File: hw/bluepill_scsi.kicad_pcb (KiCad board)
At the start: 2 copper layers, 43.8 x 73.7 mm, 14 parts, among them J1 Micro_SD_Card, J2 Conn_02x25_Odd_Even, J3 Programming Pins, J4 Berg Power Connector, U1 BluePill_STM32F103C

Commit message: Initial 1.1-a
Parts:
- added G***: LOGO, BlueSCSILogo:dogcow, B.Cu at (95.3, 160.4)
- added G***: LOGO, BlueSCSILogo:mac_happy_small, F.Cu at (95.4, 160.3)
- added G***: LOGO, BlueSCSILogo:cc_by_nc_sa_front_silk_screen, B.Cu at (103.9, 149.4)
- added G***: LOGO, BlueSCSILogo:cc_by_nc_sa_small_front_silk_screen, F.Cu at (82.8, 112.9)
- added G***: LOGO, BlueSCSILogo:BlueSCSILogoFP, B.Cu at (93.2, 126.2)
- added H2: MountingHole_Pad, MountingHole:MountingHole_2.7mm_M2.5_Pad_Via, F.Cu at (84.3, 166.5)
- added J5: Micro_SD_Card, Connector_Card:microSD_HC_Molex_104031-0811, F.Cu at (96.0, 161.0)
- added R1: R_US, Resistor_THT:R_Axial_DIN0204_L3.6mm_D1.6mm_P5.08mm_Horizontal, F.Cu at (82.4, 151.8)
- added R2: R_US, Resistor_THT:R_Axial_DIN0204_L3.6mm_D1.6mm_P5.08mm_Horizontal, F.Cu at (82.4, 144.3)
- D4, D5: moved to F.Cu
- H1: footprint MountingHole:MountingHole_2.7mm_M2.5 -> MountingHole:MountingHole_2.7mm_M2.5_Pad_Via
- J1: value Micro_SD_Card -> Berg Power Connector; footprint Connector_Card:microSD_HC_Molex_104031-0811 -> 171825-4:TE_171825-4
- J3: value Programming Pins -> ACT_LED; footprint Connector_PinHeader_2.54mm:PinHeader_1x04_P2.54mm_Vertical -> Connector_PinSocket_2.54mm:PinSocket_1x02_P2.54mm_Vertical
- J4: value Berg Power Connector -> POWER_LED; footprint 171825-4:TE_171825-4 -> Connector_PinSocket_2.54mm:PinSocket_1x02_P2.54mm_Vertical
- moved D4 87.3 mm to (105.4, 161.2)
- moved D5 80.6 mm to (105.4, 157.7)
- moved U1 73.1 mm to (101.0, 151.8), turned to 180 degrees
- moved JP1 70.5 mm to (111.1, 151.6), turned to 0 degrees
- moved JP2 70.5 mm to (107.3, 151.6), turned to 0 degrees
- moved J2 41.6 mm to (118.7, 102.2), turned to 0 degrees
- moved J1 33.5 mm to (105.2, 165.6), turned to 0 degrees
- moved H1 22.1 mm to (84.3, 98.9)
- moved J3 18.0 mm to (83.2, 161.5), turned to 90 degrees
- moved J4 17.1 mm to (83.2, 157.9), turned to 90 degrees
- moved RN3 15.3 mm to (107.3, 125.1), turned to 270 degrees
- moved RN4 15.3 mm to (111.1, 125.1), turned to 270 degrees
- moved RN1 15.3 mm to (107.3, 98.4)
- moved RN2 15.3 mm to (111.1, 98.4)
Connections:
- J1 pad 1: Net-(J1-Pad1) -> +5V
- J1 pad 2: /SD_CS -> GND
- J1 pad 3: /SD_MOSI -> (no net)
- J1 pad 4: +3V3 -> (no net)
- J2 pad 25: Net-(J2-Pad25) -> (no net)
- J2 pad 34: Net-(J2-Pad34) -> (no net)
- J3 pad 1: +3V3 -> Net-(J3-Pad1)
- J4 pad 1: +5V -> Net-(J4-Pad1)
- RN1 pad 10: /SCSI_ATN -> /SCSI_DAT7
- RN1 pad 2: /SCSI_IO -> /SCSI_DAT0
- RN1 pad 3: /SCSI_REQ -> /SCSI_DAT1
- RN1 pad 4: /SCSI_CD -> /SCSI_DAT3
- RN1 pad 5: /SCSI_MSG -> /SCSI_DAT2
- RN1 pad 6: /SCSI_BSY -> /SCSI_DBP
- RN1 pad 7: /SCSI_SEL -> /SCSI_DAT4
- RN1 pad 8: /SCSI_RST -> /SCSI_DAT5
- RN1 pad 9: /SCSI_ACK -> /SCSI_DAT6
- RN2 pad 10: /SCSI_ATN -> /SCSI_DAT7
- RN2 pad 2: /SCSI_IO -> /SCSI_DAT0
- RN2 pad 3: /SCSI_REQ -> /SCSI_DAT1
- RN2 pad 4: /SCSI_CD -> /SCSI_DAT3
- RN2 pad 5: /SCSI_MSG -> /SCSI_DAT2
- RN2 pad 6: /SCSI_BSY -> /SCSI_DBP
- RN2 pad 7: /SCSI_SEL -> /SCSI_DAT4
- RN2 pad 8: /SCSI_RST -> /SCSI_DAT5
- RN2 pad 9: /SCSI_ACK -> /SCSI_DAT6
- RN3 pad 10: /SCSI_DAT7 -> /SCSI_IO
- RN3 pad 2: /SCSI_DBP -> /SCSI_ATN
- RN3 pad 3: /SCSI_DAT0 -> /SCSI_BSY
- RN3 pad 4: /SCSI_DAT1 -> /SCSI_ACK
- RN3 pad 5: /SCSI_DAT2 -> /SCSI_RST
- RN3 pad 6: /SCSI_DAT3 -> /SCSI_MSG
- RN3 pad 7: /SCSI_DAT4 -> /SCSI_SEL
- RN3 pad 8: /SCSI_DAT5 -> /SCSI_CD
- RN3 pad 9: /SCSI_DAT6 -> /SCSI_REQ
- RN4 pad 10: /SCSI_DAT7 -> /SCSI_IO
- RN4 pad 2: /SCSI_DBP -> /SCSI_ATN
- RN4 pad 3: /SCSI_DAT0 -> /SCSI_BSY
- RN4 pad 4: /SCSI_DAT1 -> /SCSI_ACK
- RN4 pad 5: /SCSI_DAT2 -> /SCSI_RST
- RN4 pad 6: /SCSI_DAT3 -> /SCSI_MSG
- RN4 pad 7: /SCSI_DAT4 -> /SCSI_SEL
- RN4 pad 8: /SCSI_DAT5 -> /SCSI_CD
- RN4 pad 9: /SCSI_DAT6 -> /SCSI_REQ
- U1 pad 1: Net-(U1-Pad1) -> (no net)
- U1 pad 14: Net-(U1-Pad14) -> (no net)
- U1 pad 17: Net-(U1-Pad17) -> (no net)
- U1 pad 2: /LED -> (no net)
- U1 pad 28: Net-(U1-Pad28) -> (no net)
- U1 pad 29: Net-(U1-Pad29) -> (no net)
- U1 pad 3: Net-(U1-Pad3) -> (no net)
- U1 pad 4: Net-(U1-Pad4) -> (no net)
- U1 pad 5: Net-(U1-Pad5) -> /EXTERNAL_LED
- U1 pad 6: Net-(U1-Pad6) -> (no net)
- U1 pad 7: Net-(U1-Pad7) -> (no net)
- U1 pad 8: Net-(U1-Pad8) -> (no net)
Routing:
- net +5V: track 108.7 -> 9.72 mm
- net +3V3: track 85.0 -> 27.0 mm, vias 0 -> 1
- net /SCSI_BSY: track 101.0 -> 51.2 mm
- net /SCSI_ACK: track 85.7 -> 51.2 mm, vias 1 -> 0
- net /SCSI_CD: track 23.0 -> 49.1 mm
- net /SCSI_IO: track 23.0 -> 49.1 mm
- net /SCSI_REQ: track 23.4 -> 49.2 mm
- net /EXTERNAL_LED: track 0.00 -> 24.8 mm, vias 0 -> 1
- net /SCSI_RST: track 24.6 -> 49.1 mm
- net /SCSI_MSG: track 24.6 -> 49.1 mm, vias 1 -> 0
- net /TERM_PWR: track 63.5 -> 39.4 mm, vias 0 -> 1
- net /SCSI_ATN: track 26.3 -> 48.6 mm
- net /SCSI_SEL: track 27.5 -> 49.1 mm
- net Net-(J3-Pad1): track 0.00 -> 18.6 mm
- net /SCSI_DAT2: track 42.8 -> 24.8 mm, vias 1 -> 0
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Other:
- board text added: "+"
- board text added: "+3V3"
- board text added: "-"
- board text added: "12V(Y)"
- board text added: "500-1kΩ"
- board text added: "5V(R)"
- board text added: "ACT"
- board text added: "BADWOLF"
- board text added: "BERG"
- board text added: "BlueSCSI 1.1-a"
- board text added: "BlueSCSI(TM) © Eric Helgeson github.com/erichelgeson/bluescsi"
- board text added: "BlueSCSI(TM) © Eric Helgeson https://github.com/erichelgeson/bluescsi"
- board text added: "G"
- board text added: "GND"
- board text added: "LED"
- board text added: "NOT FOR COMMERCIAL SALE"
- board text added: "PA1"
- board text added: "PA4"
- board text added: "PA7"
- board text added: "PA8"
- board text added: "PB15"
- board text added: "PC13"
- board text added: "PC14"
- board text added: "PC15"
- board text added: "PWR"
- board text added: "RN1 220Ω"
- board text added: "RN2 330Ω"
- board text added: "RN3 220Ω"
- board text added: "RN4 330Ω"
- board text added: "RX2"
- board text added: "SCSI_ACK"
- board text added: "SCSI_ATN"
- board text added: "SCSI_BSY"
- board text added: "SCSI_CD"
- board text added: "SCSI_DAT0"
- board text added: "SCSI_DAT1"
- board text added: "SCSI_DAT2"
- board text added: "SCSI_DAT3"
- board text added: "SCSI_DAT4"
- board text added: "SCSI_DAT5"
- board text added: "SCSI_DAT6"
- board text added: "SCSI_DAT7"
- board text added: "SCSI_DBP"
- board text added: "SCSI_IO"
- board text added: "SCSI_MSG"
- board text added: "SCSI_REQ"
- board text added: "SCSI_RST"
- board text added: "SCSI_SEL"
- board text added: "SD_CLK"
- board text added: "SD_CS"
- board text added: "SD_MISO"
- board text added: "SD_MOSI"
- board text added: "TX2"
- board text added: "USB HERE"
- board text added: "VCC"
- board text added: "https://scsi.blue/"
- board text removed: "220"
- board text removed: "3.3 G TX RX"
- board text removed: "330"
- board text removed: "BlueSCSI 1.0-c"

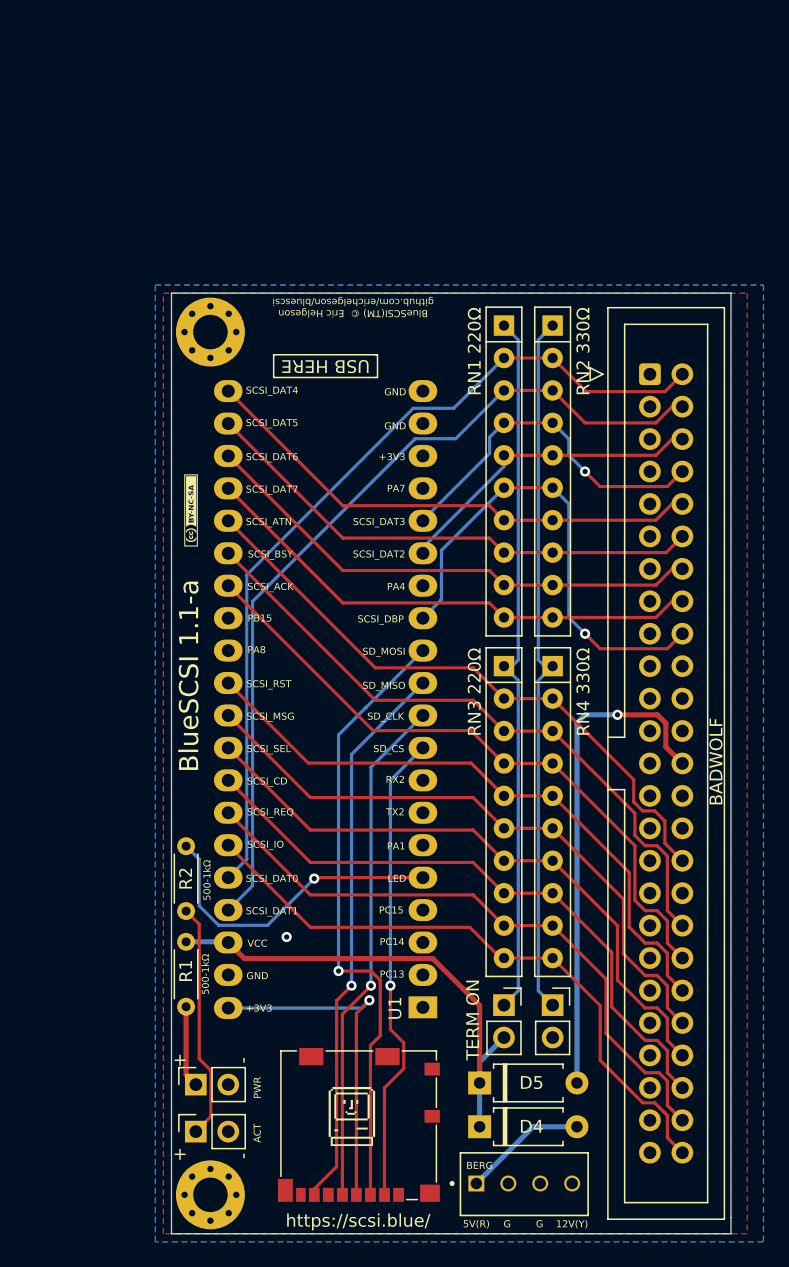
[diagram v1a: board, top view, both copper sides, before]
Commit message: bit of cleanup, flip sd card towards back
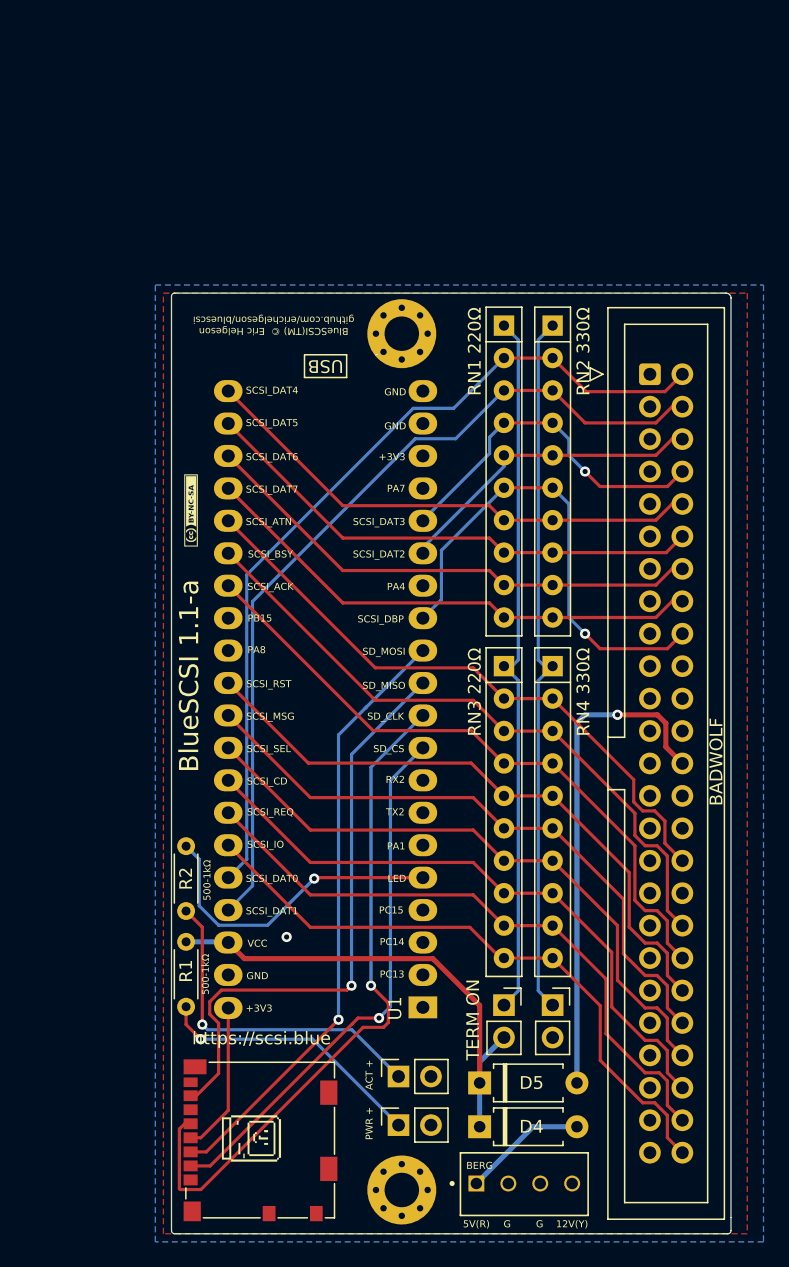
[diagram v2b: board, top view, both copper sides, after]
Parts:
- moved J3 16.5 mm to (99.1, 157.2)
- moved J4 16.2 mm to (99.1, 161.0)
- moved H2 15.0 mm to (99.3, 166.1)
- moved H1 15.0 mm to (99.3, 99.1)
- moved G*** 8.07 mm to (87.6, 162.1), turned to 270 degrees
- moved J5 7.82 mm to (88.2, 162.2), turned to 90 degrees
- moved G*** 4.72 mm to (92.1, 163.8)
- moved G*** 2.41 mm to (93.2, 128.7)
- moved G*** 1.52 mm to (103.9, 150.9)
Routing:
- net +3V3: track 27.0 -> 11.9 mm, vias 1 -> 0
- net Net-(J4-Pad1): track 6.41 -> 21.3 mm, vias 0 -> 1
- net /SD_CLK: track 40.2 -> 53.9 mm
- net Net-(J3-Pad1): track 18.6 -> 26.5 mm, vias 0 -> 1
- net /SD_CS: track 37.1 -> 42.1 mm
- net /SD_MISO: track 43.7 -> 46.5 mm
- net /SD_MOSI: track 48.7 -> 47.7 mm
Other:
- outline, holes or cut-outs redrawn
- board text added: "ACT +"
- board text added: "PWR +"
- board text added: "USB"
- board text added: "https://scsi.blue"
- board text removed: "+"
- board text removed: "ACT"
- board text removed: "PWR"
- board text removed: "USB HERE"
- board text removed: "https://scsi.blue/"
